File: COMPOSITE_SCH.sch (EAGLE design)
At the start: 10 parts, among them J1 RCALOCK, T1 BC337

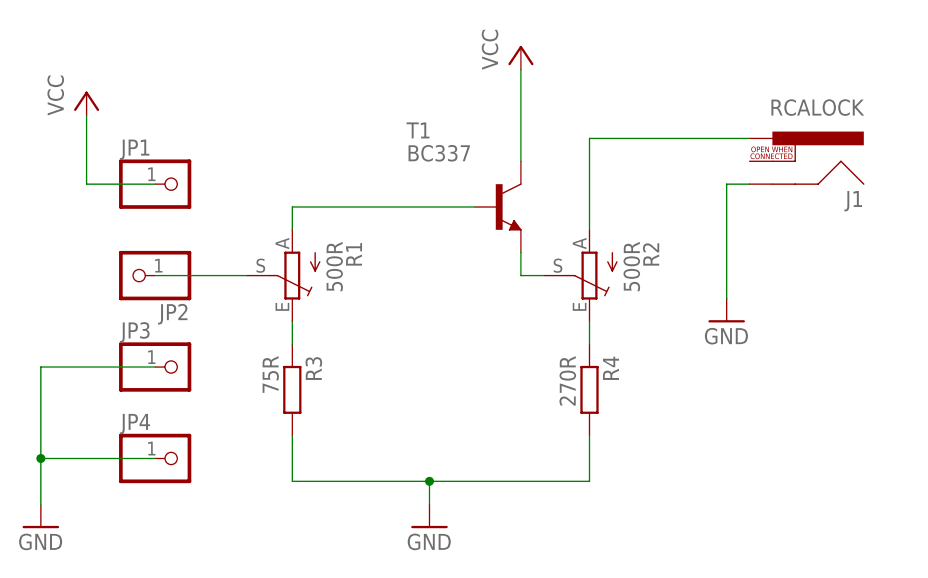
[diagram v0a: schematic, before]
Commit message: Updated design to improve video quality
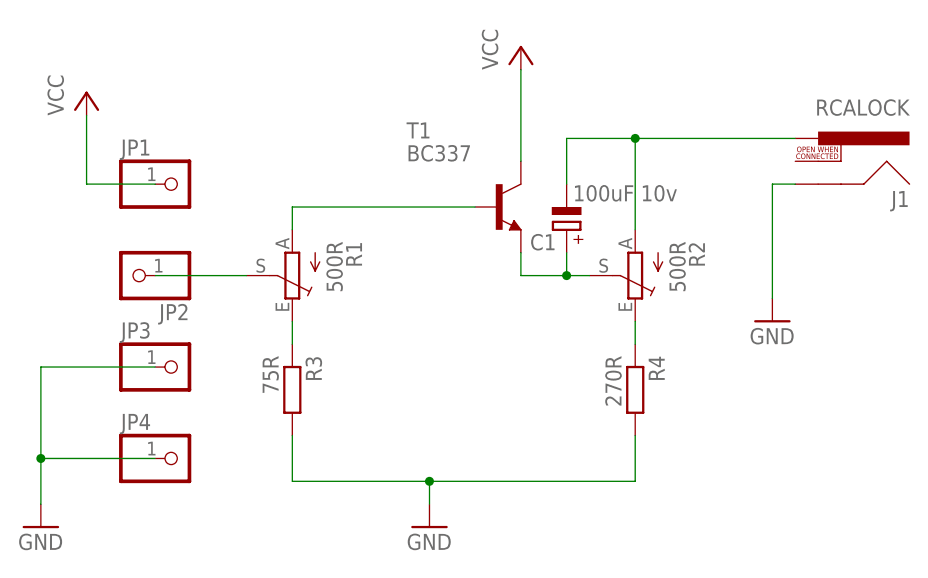
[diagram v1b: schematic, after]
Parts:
- added C1: 100uF 10v, rcl:CPOL-EUE2,5-6E
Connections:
- net N$3: now also C1.+
- net N$6: now also C1.-
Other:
- moved on the sheet: J1, R2, R4
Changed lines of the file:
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@@
 <setting verticaltext="up"/>
 </settings>
-<grid distance="0.1" unitdist="inch" unit="inch" style="lines" multiple="1" display="no" altdistance="0.01" altunitdist="inch" altunit="inch"/>
+<grid distance="0.001" unitdist="inch" unit="inch" style="lines" multiple="1" display="no" altdistance="0.01" altunitdist="inch" altunit="inch"/>
 <layers>
 <layer number="1" name="Top" color="4" fill="1" visible="no" active="no"/>
@@
 <part name="JP4" library="pinhead" library_urn="urn:adsk.eagle:library:325" deviceset="PINHD-1X1" device="" package3d_urn="urn:adsk.eagle:package:22485/2"/>
 <part name="GND3" library="supply1" library_urn="urn:adsk.eagle:library:371" deviceset="GND" device=""/>
+<part name="C1" library="rcl" library_urn="urn:adsk.eagle:library:334" deviceset="CPOL-EU" device="E2,5-6E" package3d_urn="urn:adsk.eagle:package:23430/1" value="100uF 10v"/>
 </parts>
 <sheets>
@@
 <attribute name="VALUE" x="52.07" y="54.61" size="1.778" layer="96" rot="R270"/>
 </instance>
-<instance part="R2" gate="1" x="81.28" y="50.8" smashed="yes" rot="R180">
-<attribute name="NAME" x="87.249" y="54.61" size="1.778" layer="95" rot="R270"/>
-<attribute name="VALUE" x="85.09" y="54.61" size="1.778" layer="96" rot="R270"/>
+<instance part="R2" gate="1" x="86.36" y="50.8" smashed="yes" rot="R180">
+<attribute name="NAME" x="92.329" y="54.61" size="1.778" layer="95" rot="R270"/>
+<attribute name="VALUE" x="90.17" y="54.61" size="1.778" layer="96" rot="R270"/>
 </instance>
 <instance part="T1" gate="G$1" x="71.12" y="58.42" smashed="yes">
@@
 <attribute name="VALUE" x="44.958" y="41.91" size="1.778" layer="96" rot="R270"/>
 </instance>
-<instance part="R4" gate="G$1" x="81.28" y="38.1" smashed="yes" rot="R270">
-<attribute name="NAME" x="82.7786" y="41.91" size="1.778" layer="95" rot="R270"/>
-<attribute name="VALUE" x="77.978" y="41.91" size="1.778" layer="96" rot="R270"/>
-</instance>
-<instance part="J1" gate="G$1" x="99.06" y="63.5" smashed="yes" rot="MR0">
-<attribute name="VALUE" x="111.76" y="68.58" size="1.778" layer="96" font="vector" rot="MR0"/>
-<attribute name="NAME" x="111.76" y="58.42" size="1.778" layer="95" font="vector" rot="MR0"/>
-</instance>
-<instance part="GND1" gate="1" x="96.52" y="45.72" smashed="yes">
-<attribute name="VALUE" x="93.98" y="43.18" size="1.778" layer="96"/>
+<instance part="R4" gate="G$1" x="86.36" y="38.1" smashed="yes" rot="R270">
+<attribute name="NAME" x="87.8586" y="41.91" size="1.778" layer="95" rot="R270"/>
+<attribute name="VALUE" x="83.058" y="41.91" size="1.778" layer="96" rot="R270"/>
+</instance>
+<instance part="J1" gate="G$1" x="104.14" y="63.5" smashed="yes" rot="MR0">
+<attribute name="VALUE" x="116.84" y="68.58" size="1.778" layer="96" font="vector" rot="MR0"/>
+<attribute name="NAME" x="116.84" y="58.42" size="1.778" layer="95" font="vector" rot="MR0"/>
+</instance>
+<instance part="GND1" gate="1" x="101.6" y="45.72" smashed="yes">
+<attribute name="VALUE" x="99.06" y="43.18" size="1.778" layer="96"/>
 </instance>
 <instance part="GND2" gate="1" x="63.5" y="22.86" smashed="yes">
@@
 <instance part="GND3" gate="1" x="20.32" y="22.86" smashed="yes">
 <attribute name="VALUE" x="17.78" y="20.32" size="1.778" layer="96"/>
+</instance>
+<instance part="C1" gate="G$1" x="78.74" y="55.88" smashed="yes" rot="R180">
+<attribute name="NAME" x="77.597" y="55.3974" size="1.778" layer="95" rot="R180"/>
+<attribute name="VALUE" x="79.4258" y="59.055" size="1.778" layer="96"/>
 </instance>
 </instances>
@@
 <wire x1="73.66" y1="53.34" x2="73.66" y2="50.8" width="0.1524" layer="91"/>
 <pinref part="R2" gate="1" pin="S"/>
-<wire x1="73.66" y1="50.8" x2="76.2" y2="50.8" width="0.1524" layer="91"/>
+<wire x1="73.66" y1="50.8" x2="78.74" y2="50.8" width="0.1524" layer="91"/>
+<pinref part="C1" gate="G$1" pin="+"/>
+<wire x1="78.74" y1="50.8" x2="81.28" y2="50.8" width="0.1524" layer="91"/>
+<wire x1="78.74" y1="53.34" x2="78.74" y2="50.8" width="0.1524" layer="91"/>
+<junction x="78.74" y="50.8"/>
 </segment>
 </net>
@@
 <pinref part="R2" gate="1" pin="E"/>
 <pinref part="R4" gate="G$1" pin="1"/>
-<wire x1="81.28" y1="45.72" x2="81.28" y2="43.18" width="0.1524" layer="91"/>
+<wire x1="86.36" y1="45.72" x2="86.36" y2="43.18" width="0.1524" layer="91"/>
 </segment>
 </net>
@@
 <segment>
 <pinref part="R2" gate="1" pin="A"/>
-<wire x1="81.28" y1="66.04" x2="81.28" y2="55.88" width="0.1524" layer="91"/>
+<wire x1="86.36" y1="66.04" x2="86.36" y2="55.88" width="0.1524" layer="91"/>
 <pinref part="J1" gate="G$1" pin="PIN"/>
-<wire x1="99.06" y1="66.04" x2="81.28" y2="66.04" width="0.1524" layer="91"/>
+<wire x1="104.14" y1="66.04" x2="86.36" y2="66.04" width="0.1524" layer="91"/>
+<pinref part="C1" gate="G$1" pin="-"/>
+<wire x1="78.74" y1="60.96" x2="78.74" y2="66.04" width="0.1524" layer="91"/>
+<wire x1="78.74" y1="66.04" x2="86.36" y2="66.04" width="0.1524" layer="91"/>
+<junction x="86.36" y="66.04"/>
 </segment>
 </net>
@@
 <net name="GND" class="0">
 <segment>
-<wire x1="96.52" y1="60.96" x2="96.52" y2="48.26" width="0.1524" layer="91"/>
+<wire x1="101.6" y1="60.96" x2="101.6" y2="48.26" width="0.1524" layer="91"/>
 <pinref part="GND1" gate="1" pin="GND"/>
 <pinref part="J1" gate="G$1" pin="SHELL"/>
-<wire x1="99.06" y1="60.96" x2="96.52" y2="60.96" width="0.1524" layer="91"/>
+<wire x1="104.14" y1="60.96" x2="101.6" y2="60.96" width="0.1524" layer="91"/>
 </segment>
 <segment>
@@
 <wire x1="48.26" y1="27.94" x2="63.5" y2="27.94" width="0.1524" layer="91"/>
 <pinref part="R4" gate="G$1" pin="2"/>
-<wire x1="63.5" y1="27.94" x2="81.28" y2="27.94" width="0.1524" layer="91"/>
-<wire x1="81.28" y1="27.94" x2="81.28" y2="33.02" width="0.1524" layer="91"/>
+<wire x1="63.5" y1="27.94" x2="86.36" y2="27.94" width="0.1524" layer="91"/>
+<wire x1="86.36" y1="27.94" x2="86.36" y2="33.02" width="0.1524" layer="91"/>
 <pinref part="GND2" gate="1" pin="GND"/>
 <wire x1="63.5" y1="25.4" x2="63.5" y2="27.94" width="0.1524" layer="91"/>
@@
 </sheet>
 </sheets>
+<errors>
+</errors>
 </schematic>
 </drawing>
